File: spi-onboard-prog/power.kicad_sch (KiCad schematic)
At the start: 13 parts, among them P3 CBMTAPE

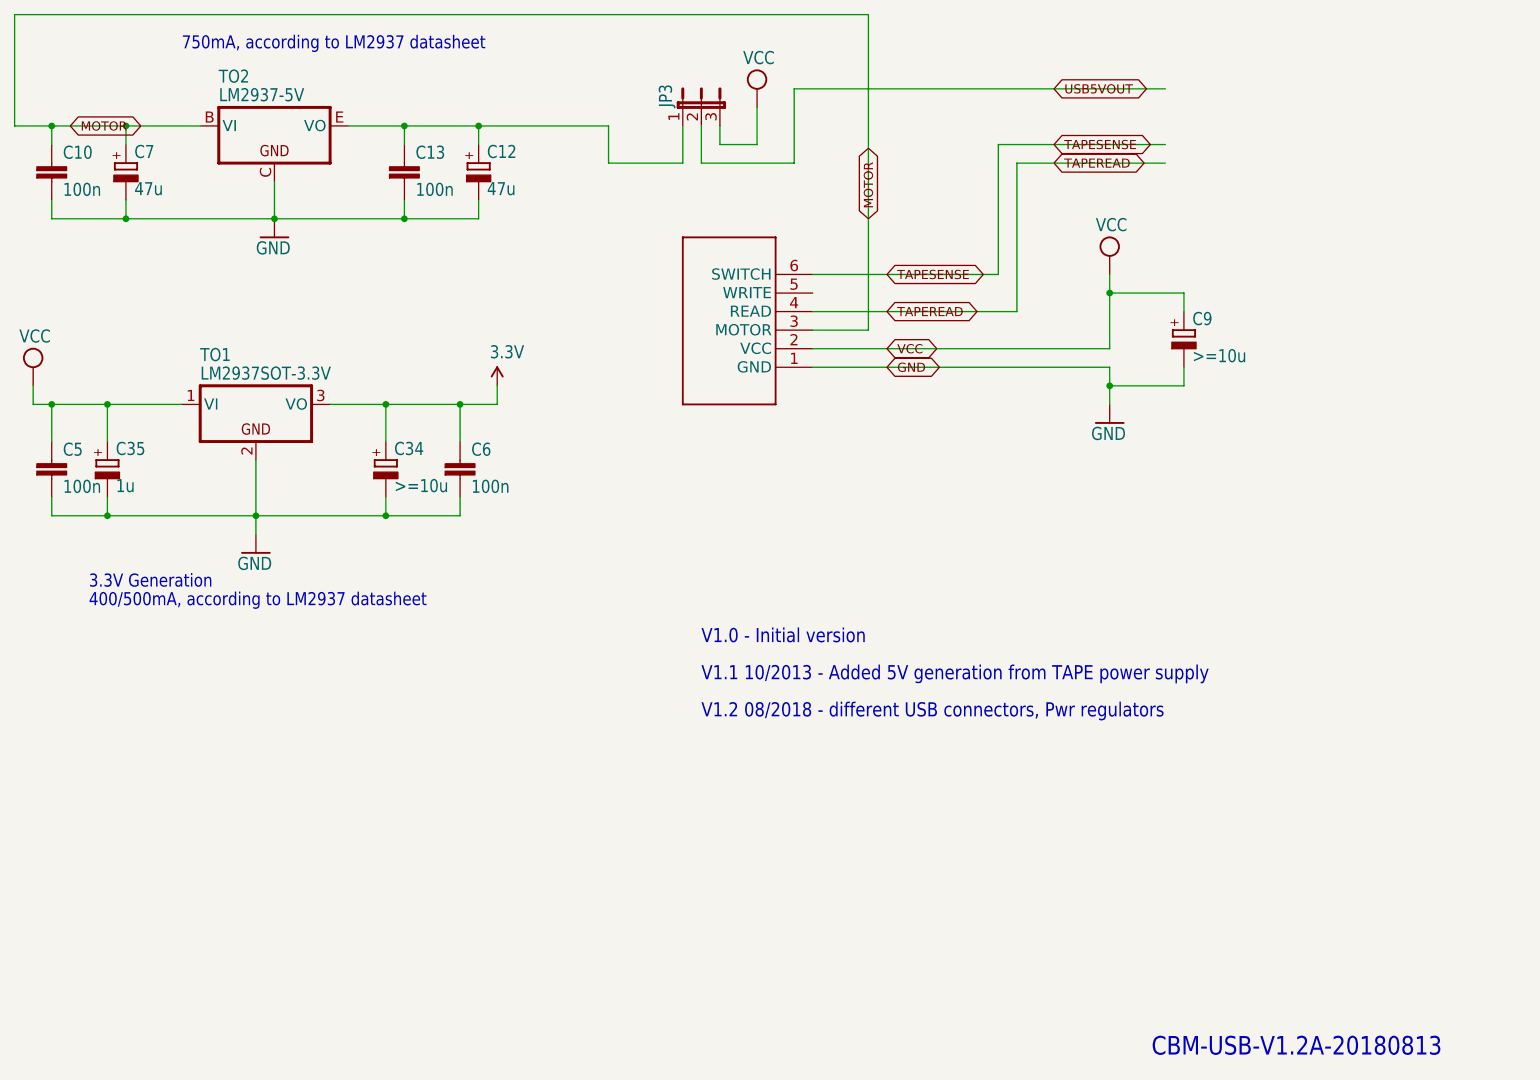
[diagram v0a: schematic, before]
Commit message: layout work on onboard spi prog
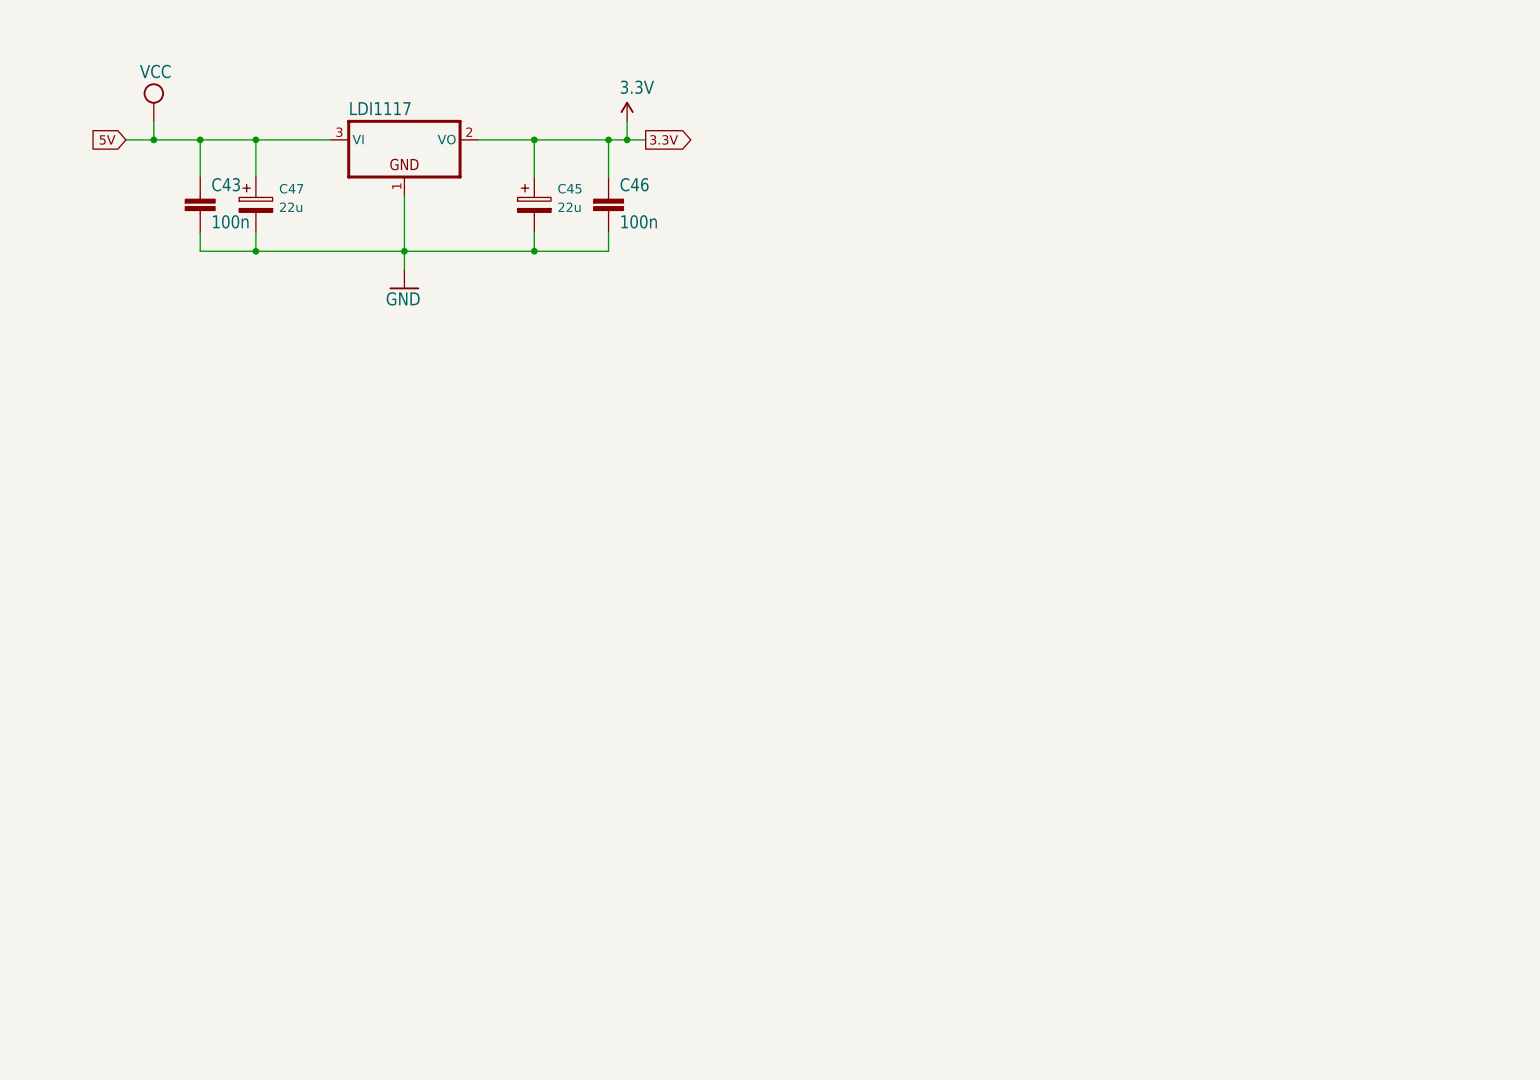
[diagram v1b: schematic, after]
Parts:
- removed C10, C13: 100n, cbm_usb_v1-import-fps:C050-030X075, symbol cbm_usb_v1-eagle-import:C-EU050-030X075
- removed C12, C7: 47u, cbm_usb_v1-import-fps:E3,5-8, symbol cbm_usb_v1-eagle-import:CPOL-EUE3.5-8
- removed C34: >=10u, cbm_usb_v1-import-fps:E5-8,5, symbol cbm_usb_v1-eagle-import:CPOL-EUE5-8.5
- removed C35: 1u, cbm_usb_v1-import-fps:E5-8,5, symbol cbm_usb_v1-eagle-import:CPOL-EUE5-8.5
- removed C5, C6: 100n, cbm_usb_v1-import-fps:C050-025X075, symbol cbm_usb_v1-eagle-import:C-EU050-025X075
- removed C9: >=10u, cbm_usb_v1-import-fps:E5-10,5, symbol cbm_usb_v1-eagle-import:CPOL-EUE5-10.5
- removed JP3: JP2E, cbm_usb_v1-import-fps:JP2, symbol cbm_usb_v1-eagle-import:JP2E
- removed P3: CBMTAPE, cbm_usb_v1-import-fps:JP6, symbol cbm_usb_v1-eagle-import:CBMTAPE
- removed TO1: LM2937SOT-3.3V, cbm_usb_v1-import-fps:SOT223, symbol cbm_usb_v1-eagle-import:LM2937SOT
- removed TO2: LM2937-5V, cbm_usb_v1-import-fps:TO220H, symbol cbm_usb_v1-eagle-import:LM2937
- added C43, C46: 100n, Capacitor_SMD:C_0603_1608Metric_Pad1.08x0.95mm_HandSolder, symbol cbm_ultipet_v1-eagle-import:C-EUC0603
- added C45, C47: 22u, Capacitor_SMD:C_1206_3216Metric_Pad1.33x1.80mm_HandSolder, symbol Device:C_Polarized
- added UX3: LDI1117, Package_TO_SOT_SMD:SOT-223, symbol cbm_ultipet_v1-eagle-import:LDI1117
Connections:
- net 3.3V: now also C45.1, C46.1, UX3.2 (VO)
- net GND: now also C43.2, C45.2, C46.2, C47.2, UX3.1 (GND)
- net VCC: now also C43.1, C47.1, UX3.3 (VI)
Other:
- note removed: "3.3V Generation"
- note removed: "400/500mA, according to LM2937 datasheet"
- note removed: "750mA, according to LM2937 datasheet"
- note removed: "CBM-USB-V1.2A-20180813"
- note removed: "V1.0 - Initial version"
- note removed: "V1.1 10/2013 - Added 5V generation from TAPE power supply"
- note removed: "V1.2 08/2018 - different USB connectors, Pwr regulators"

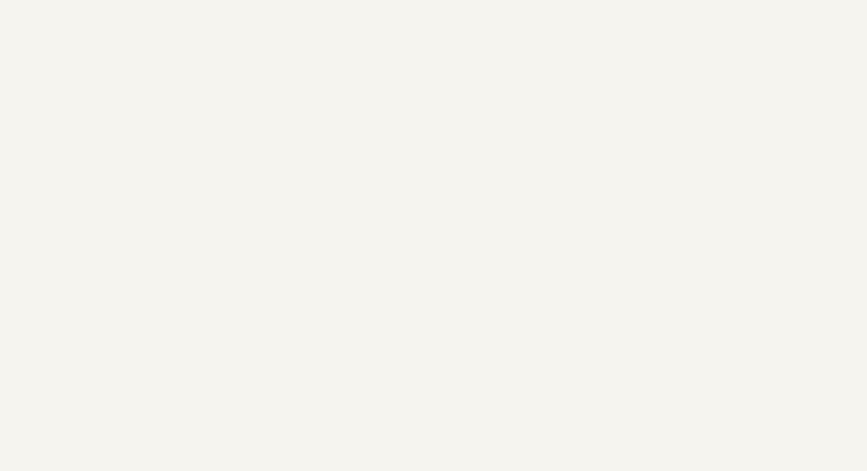
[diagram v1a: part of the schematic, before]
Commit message: move spi onboard prog to draft spi userport
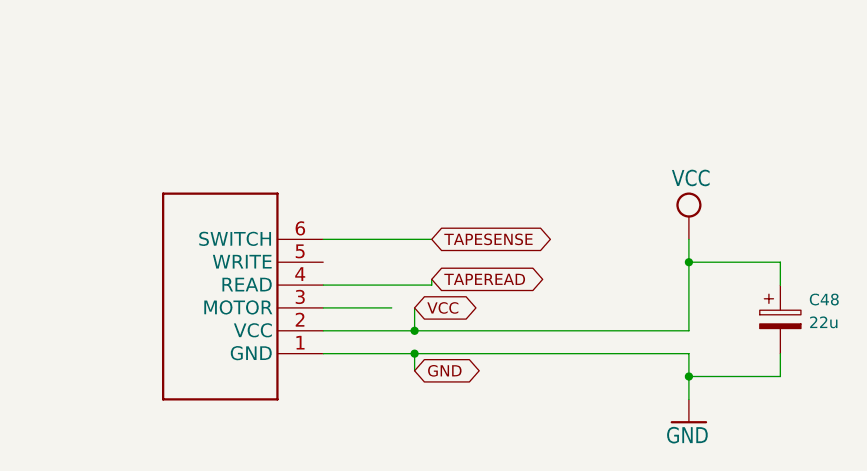
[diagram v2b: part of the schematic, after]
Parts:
- added C48: 22u, Capacitor_SMD:C_1206_3216Metric_Pad1.33x1.80mm_HandSolder, symbol Device:C_Polarized
- added P3: CBMTAPE, Connector_PinHeader_2.54mm:PinHeader_1x06_P2.54mm_Vertical, symbol cbm_usb_v1-eagle-import:CBMTAPE
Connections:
- net GND: now also C48.2, P3.1 (GND)
- net VCC: now also C48.1, P3.2 (VCC)
- new net TAPEREAD: P3.4 (READ)
- new net TAPESENSE: P3.6 (SWITCH)

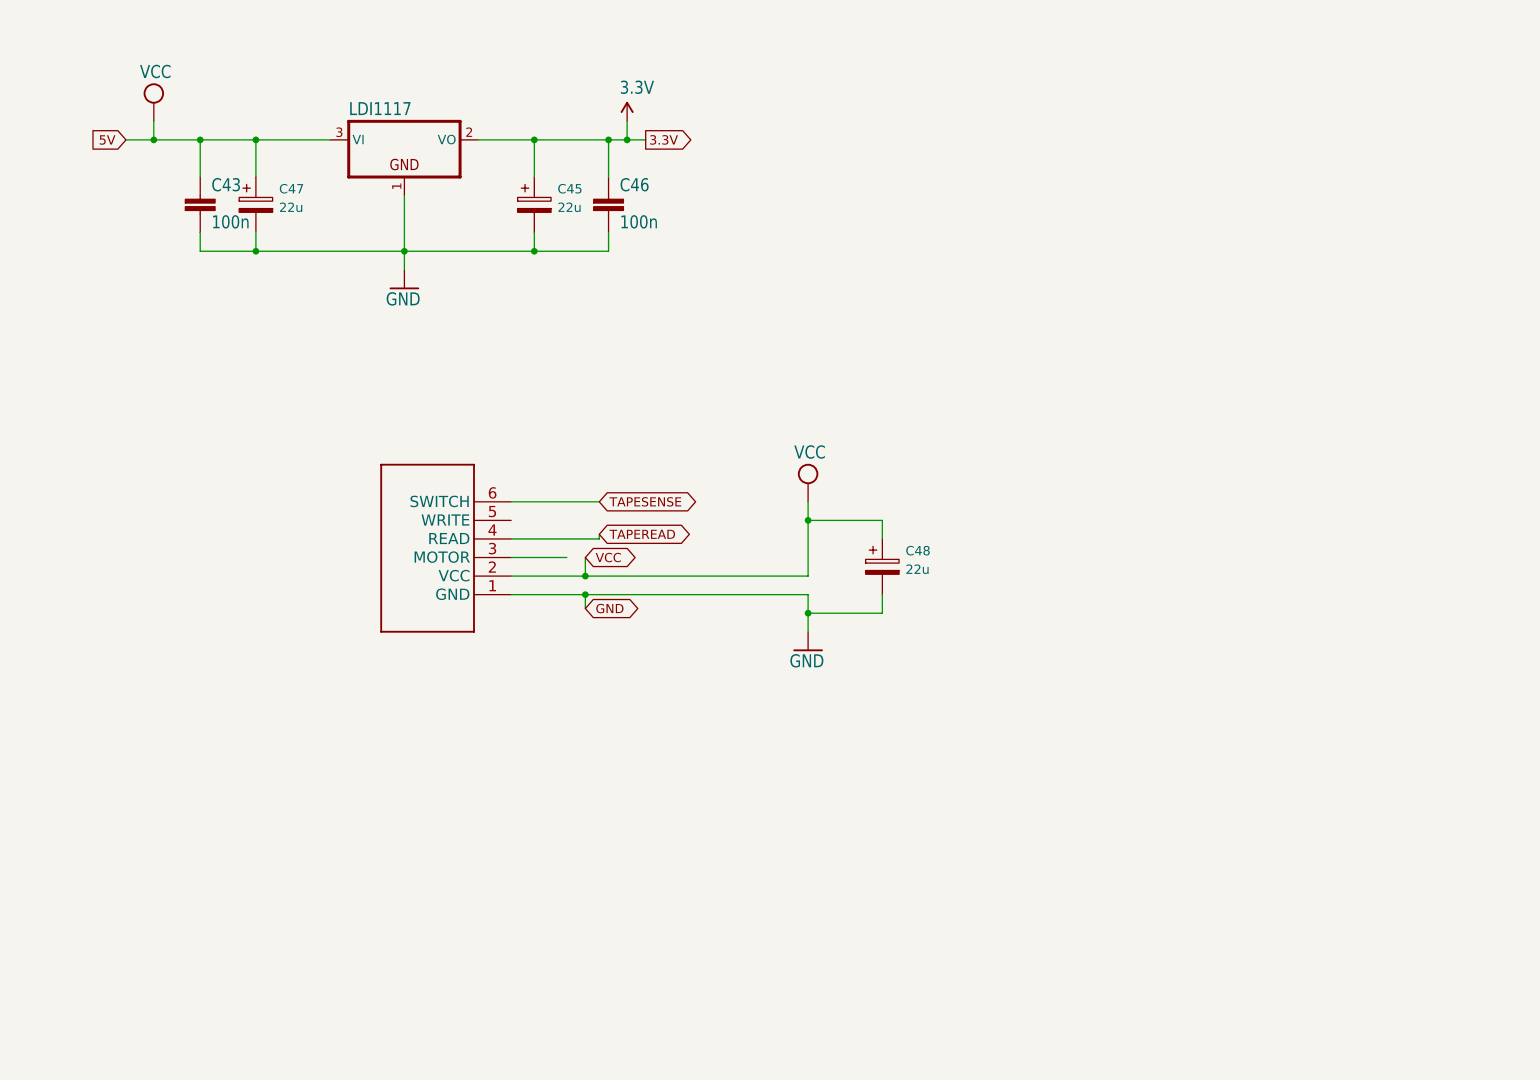
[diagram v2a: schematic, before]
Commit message: onboard prog on SPI10-3.3V
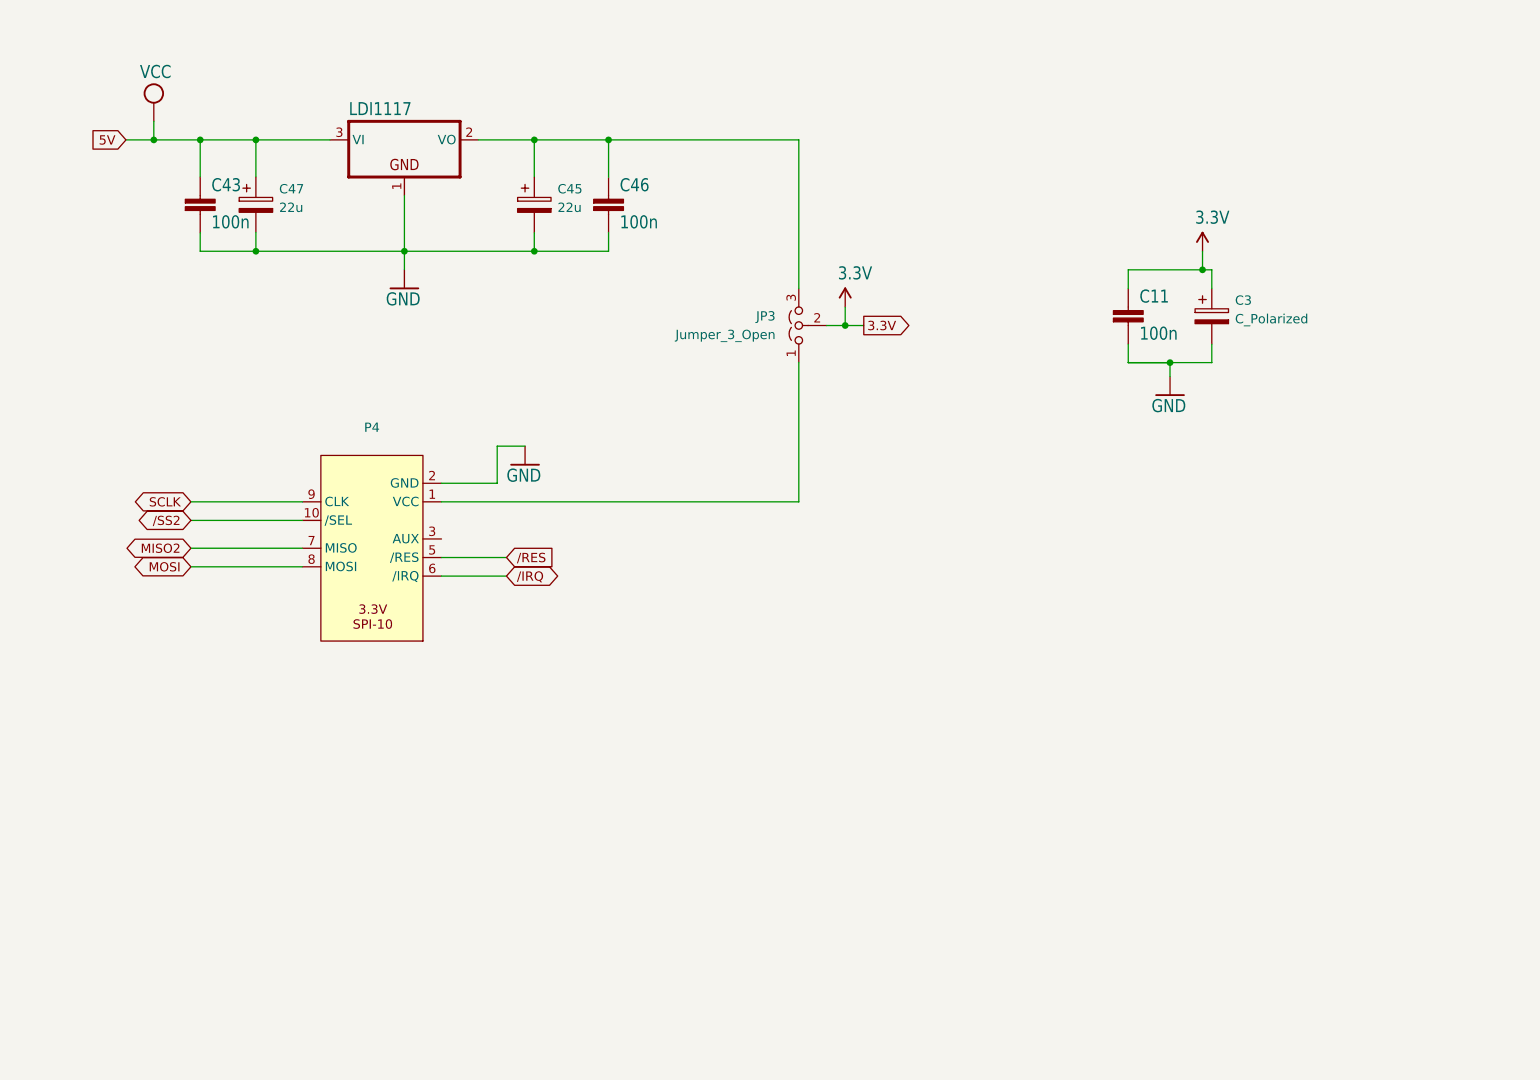
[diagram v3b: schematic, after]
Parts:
- removed C48: 22u, Capacitor_SMD:C_1206_3216Metric_Pad1.33x1.80mm_HandSolder, symbol Device:C_Polarized
- removed P3: CBMTAPE, Connector_PinHeader_2.54mm:PinHeader_1x06_P2.54mm_Vertical, symbol cbm_usb_v1-eagle-import:CBMTAPE
- added C11: 100n, Capacitor_SMD:C_0603_1608Metric_Pad1.08x0.95mm_HandSolder, symbol cbm_usb_v1-eagle-import:C-EU050-025X075
- added C3: C_Polarized, Capacitor_SMD:C_1206_3216Metric_Pad1.33x1.80mm_HandSolder, symbol Device:C_Polarized
- added JP3: Jumper_3_Open, Connector_PinHeader_2.54mm:PinHeader_1x03_P2.54mm_Vertical, symbol Jumper:Jumper_3_Open
- added P4: (no value), Connector_IDC:IDC-Header_2x05_P2.54mm_Vertical, symbol SPI:SPI-10-3V3
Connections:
- net 3.3V: now also C11.1, C3.1, JP3.2 (C); no longer C45.1, C46.1, UX3.2 (VO)
- net GND: now also C11.2, C3.2, P4.2 (GND)
- new net: C45.1, C46.1, JP3.3 (B), UX3.2 (VO)
- new net: JP3.1 (A), P4.1 (VCC)
- new net /SS2: P4.10 (/SEL)
- new net MISO2: P4.7 (MISO)
- new net MOSI: P4.8 (MOSI)
- new net SCLK: P4.9 (CLK)
- new net /IRQ: P4.6 (/IRQ)
- new net /RES: P4.5 (/RES)

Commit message: onboard flash prog
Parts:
- C3: value C_Polarized -> 47u
- C45, C47: value 22u -> 47u; LCSC C12891 -> (none)
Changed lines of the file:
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@@
 			)
 		)
-		(property "Value" "C_Polarized"
+		(property "Value" "47u"
 			(at 230.505 85.4709 0)
 			(show_name no)
@@
 			)
 		)
-		(property "Value" "22u"
+		(property "Value" "47u"
 			(at 99.695 70.2309 0)
 			(show_name no)
@@
 			)
 		)
-		(property "LCSC" "C12891"
+		(property "LCSC" ""
 			(at 99.695 67.6909 0)
 			(hide yes)
@@
 			)
 		)
-		(property "Value" "22u"
+		(property "Value" "47u"
 			(at 137.795 70.2309 0)
 			(show_name no)
@@
 			)
 		)
-		(property "LCSC" "C12891"
+		(property "LCSC" ""
 			(at 137.795 67.6909 0)
 			(hide yes)
